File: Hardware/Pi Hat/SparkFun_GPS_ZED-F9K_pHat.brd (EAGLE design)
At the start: 65 x 57.3 mm, 113 parts, among them J1 QWIIC_RIGHT_ANGLE, J2 RASPBERRYPI-40-PIN-GPIO_SMD_S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, J4 U.FL, U1 UBLOX_ZED_F9R, U2 HCPL-270L

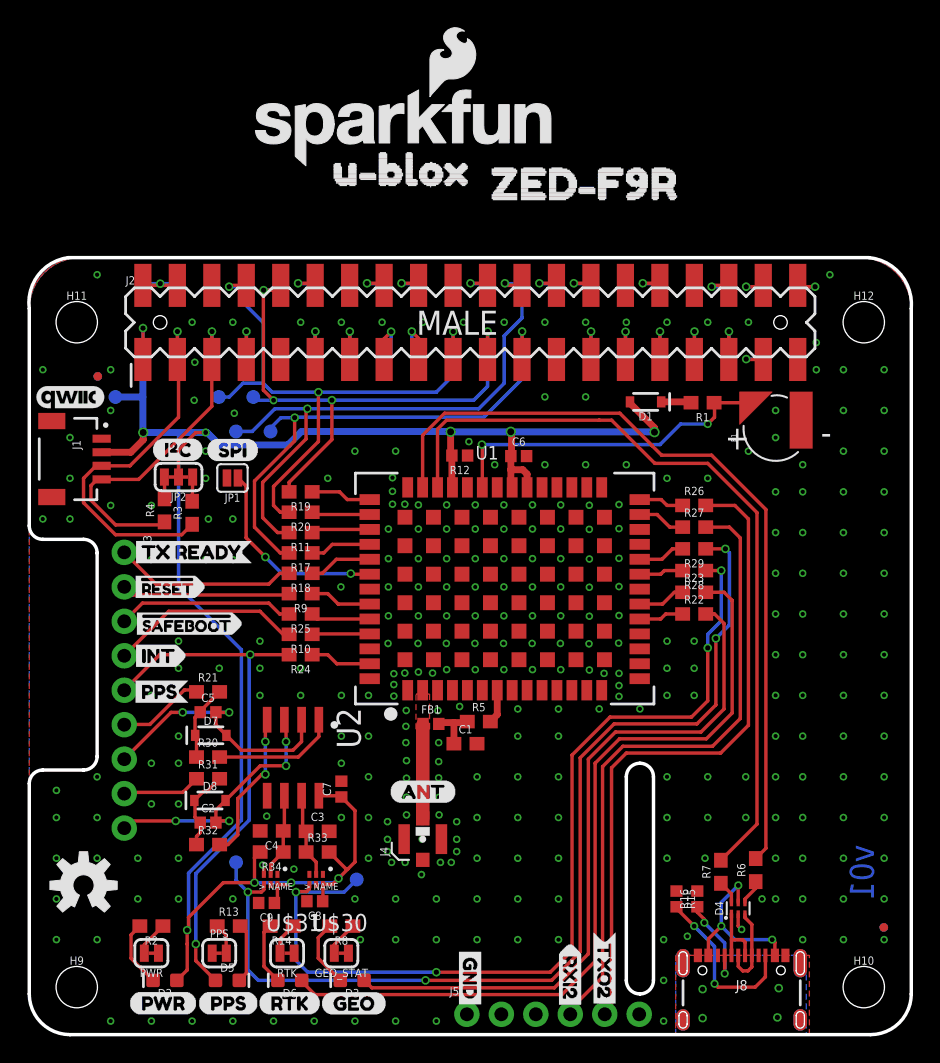
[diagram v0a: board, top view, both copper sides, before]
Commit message: Adds automotive certified diode to wt/dir circuitry
* Adds wt/dir circuitry to both breakout board and pi hat
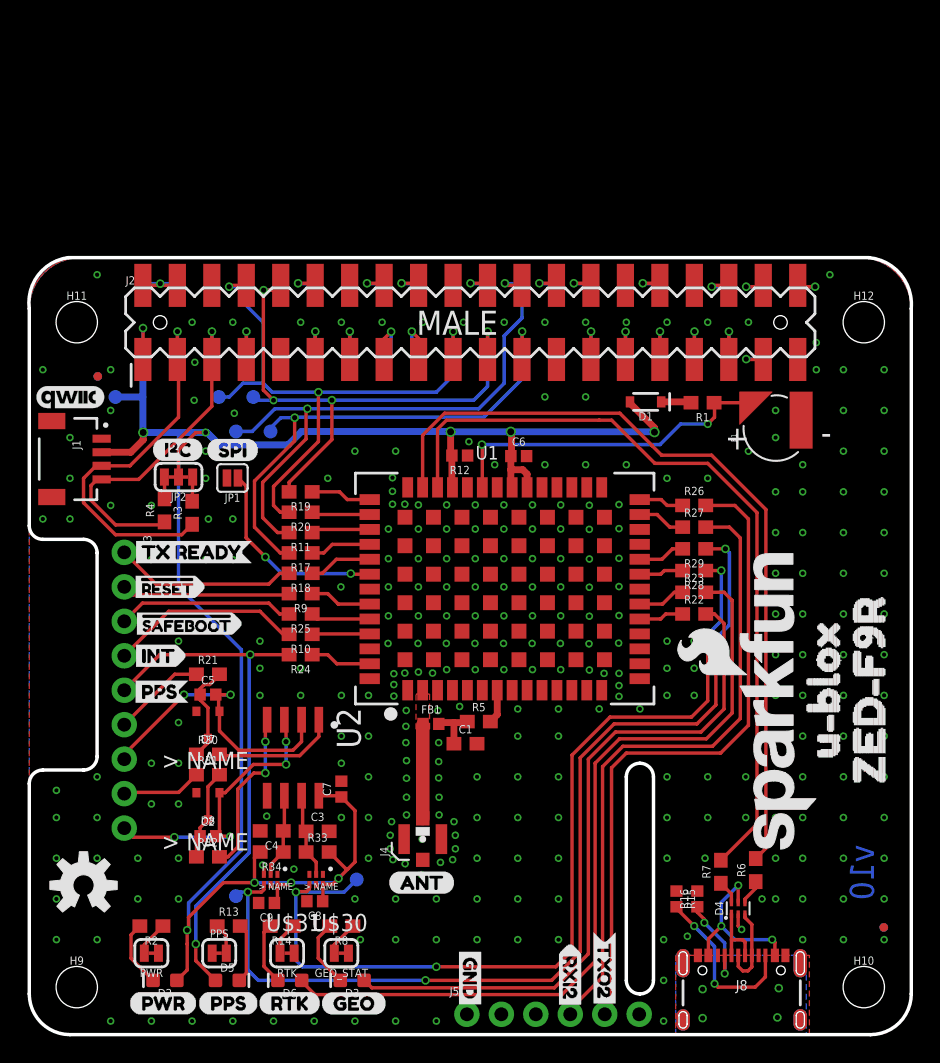
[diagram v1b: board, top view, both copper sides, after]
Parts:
- D7, D8: device SparkFun-DiscreteSemi:SOD-323 -> classified:SOT23_BZX
- moved U$25 59.5 mm to (58.6, 18.3), turned to 90 degrees
- moved U$26 55.0 mm to (61.9, 16.5), turned to 90 degrees
- moved LOGO1 50.4 mm to (55.1, 24.6), turned to 90 degrees
- moved U$21 6.70 mm to (26.4, 11.2)
- moved TP7 2.49 mm to (15.2, 10.2)
- moved R21 1.30 mm to (13.2, 26.6)
- moved C5 1.30 mm to (13.2, 25.1)
- moved C2 1.00 mm to (13.2, 14.6)
- moved R32 0.90 mm to (13.2, 13.1)
- moved D7 0.81 mm to (13.2, 22.8), turned to 180 degrees
- moved D8 0.44 mm to (13.2, 16.8), turned to 180 degrees
- moved R31 0.30 mm to (13.2, 19.2)
- moved R30 0.20 mm to (13.2, 20.7)
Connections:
- net DIR-: now also D8.P1; no longer D8.A
- net N$27: now also D7.P3; no longer D7.C
- net N$36: now also D8.P3; no longer D8.C
- net WT-: now also D7.P1; no longer D7.A
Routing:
- net WT-: track 20.0 -> 22.4 mm
- net DIR-: track 19.9 -> 21.7 mm
- net N$27: track 5.60 -> 7.39 mm
- net DIR_OUT: track 75.0 -> 73.5 mm
- net DIR_IN: track 11.2 -> 12.4 mm
- net N$36: track 6.08 -> 6.91 mm
- net GND: vias 303 -> 299
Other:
- board text added: "v10"
- board text removed: "v01"

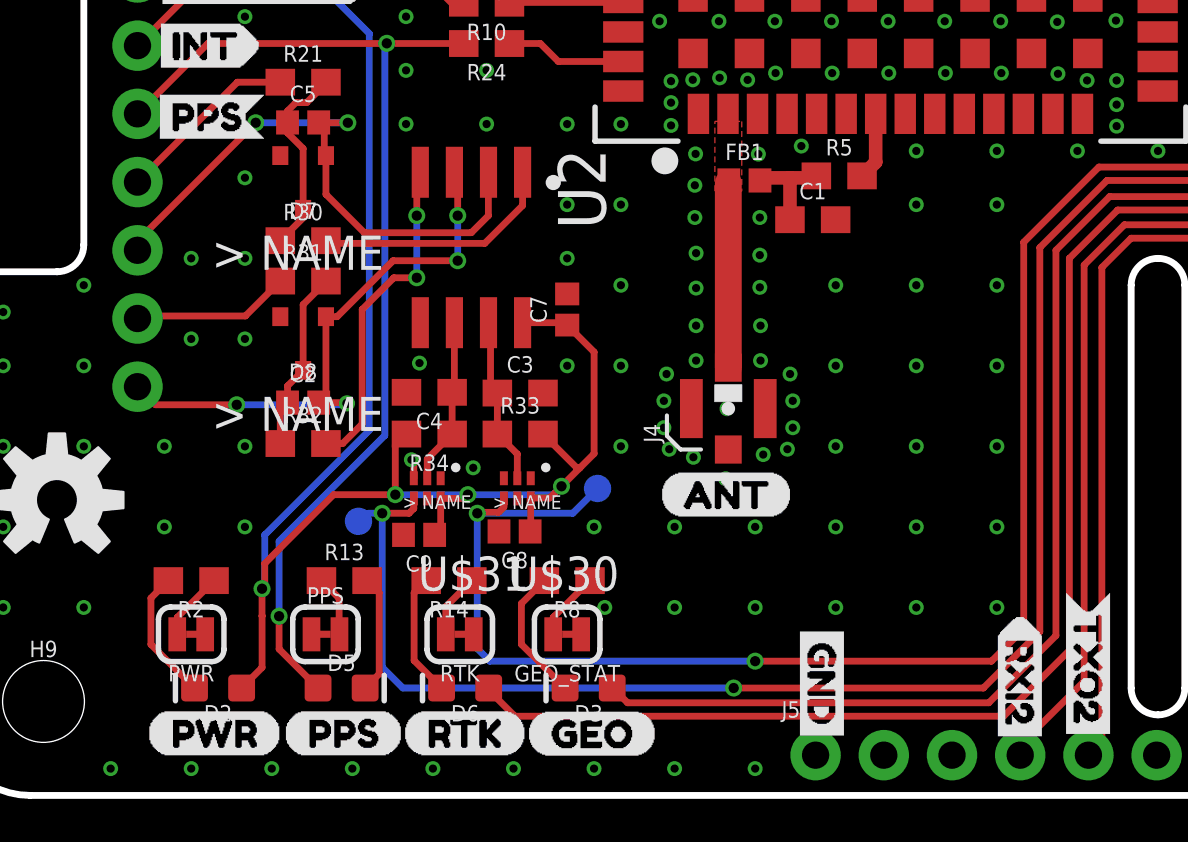
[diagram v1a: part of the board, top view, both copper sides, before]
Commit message: Adds labels for new PTH for wt/dir lines
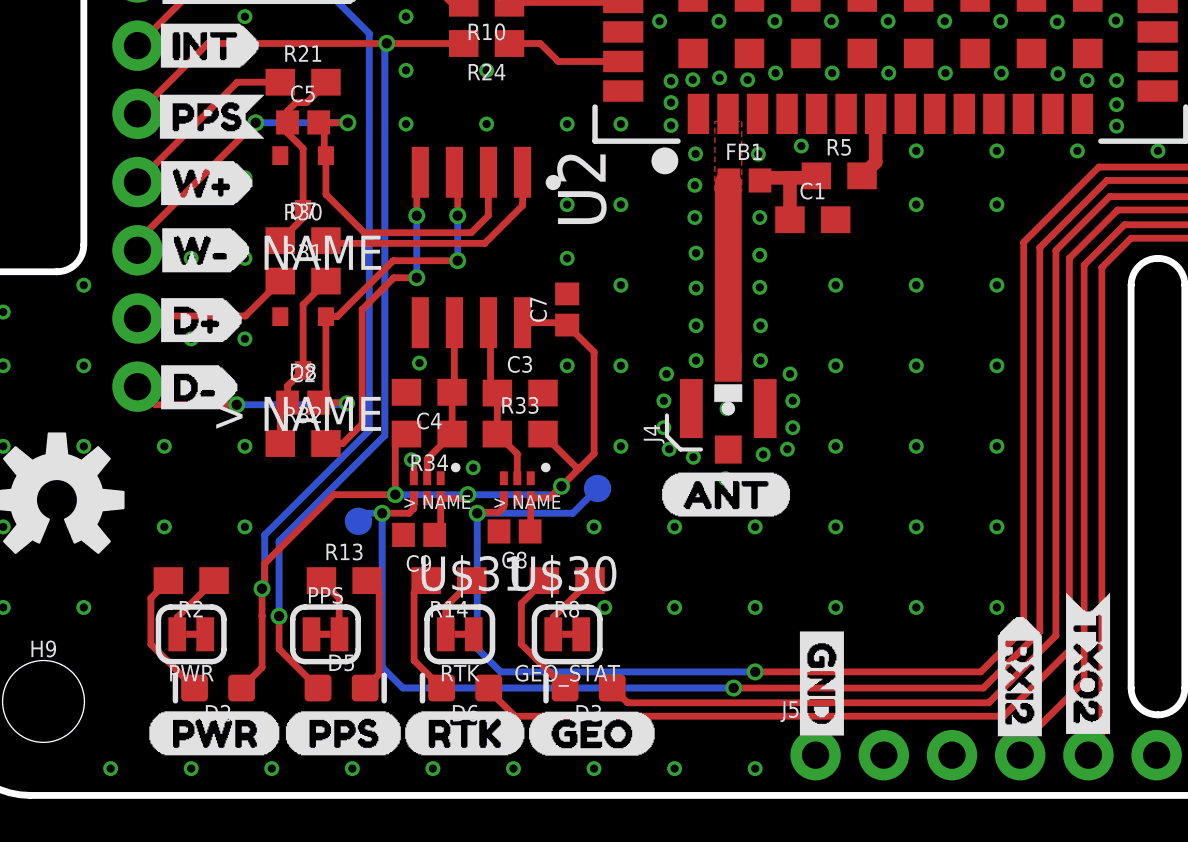
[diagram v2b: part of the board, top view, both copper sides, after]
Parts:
- added U$22: (no value), wt_dir_top:D#0
- added U$23: (no value), wt_dir_top:D#1
- added U$27: (no value), wt_dir_top:W#2
- added U$28: (no value), wt_dir_top:W#3
- added U$32: (no value), wt_dir:D#0
- added U$33: (no value), wt_dir:D#1
- added U$34: (no value), wt_dir:W#2
- added U$35: (no value), wt_dir:W#3
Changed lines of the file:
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@@
 <layer number="19" name="Unrouted" color="6" fill="1" visible="yes" active="yes"/>
 <layer number="20" name="Dimension" color="15" fill="1" visible="yes" active="yes"/>
-<layer number="21" name="tPlace" color="16" fill="1" visible="no" active="yes"/>
-<layer number="22" name="bPlace" color="14" fill="1" visible="no" active="yes"/>
+<layer number="21" name="tPlace" color="16" fill="1" visible="yes" active="yes"/>
+<layer number="22" name="bPlace" color="14" fill="1" visible="yes" active="yes"/>
 <layer number="23" name="tOrigins" color="15" fill="1" visible="yes" active="yes"/>
 <layer number="24" name="bOrigins" color="15" fill="1" visible="yes" active="yes"/>
@@
 <layer number="37" name="tTest" color="7" fill="1" visible="no" active="yes"/>
 <layer number="38" name="bTest" color="7" fill="1" visible="no" active="yes"/>
-<layer number="39" name="tKeepout" color="4" fill="11" visible="yes" active="yes"/>
+<layer number="39" name="tKeepout" color="4" fill="11" visible="no" active="yes"/>
 <layer number="40" name="bKeepout" color="1" fill="11" visible="no" active="yes"/>
 <layer number="41" name="tRestrict" color="4" fill="10" visible="no" active="yes"/>
@@
 <element name="TP6" library="SparkFun-Connectors" package="PAD.03X.04" value="TEST-POINT3X4" x="24.13" y="11.43" smashed="yes" rot="MR270"/>
 <element name="TP7" library="SparkFun-Connectors" package="PAD.03X.04" value="TEST-POINT3X4" x="15.229" y="10.208" smashed="yes" rot="MR270"/>
+<element name="U$22" library="wt_dir_top" package="D#0" value="" x="7.4" y="17.7" smashed="yes"/>
+<element name="U$23" library="wt_dir_top" package="D#1" value="" x="7.4" y="15.2" smashed="yes"/>
+<element name="U$27" library="wt_dir_top" package="W#2" value="" x="7.4" y="22.8" smashed="yes"/>
+<element name="U$28" library="wt_dir_top" package="W#3" value="" x="7.4" y="20.3" smashed="yes"/>
+<element name="U$35" library="wt_dir" package="W#3" value="" x="11.2" y="20.3" smashed="yes" rot="MR0"/>
+<element name="U$32" library="wt_dir" package="D#0" value="" x="10.9" y="15.2" smashed="yes" rot="MR0"/>
+<element name="U$33" library="wt_dir" package="D#1" value="" x="10.8" y="17.7" smashed="yes" rot="MR0"/>
+<element name="U$34" library="wt_dir" package="W#2" value="" x="11.3" y="22.8" smashed="yes" rot="MR0"/>
 </elements>
 <signals>
@@
 <wire x1="48.8" y1="23.4" x2="42.8" y2="23.4" width="0.254" layer="1"/>
 <wire x1="40" y1="20.6" x2="40" y2="6.2" width="0.254" layer="1"/>
-<wire x1="40" y1="6.2" x2="38.8" y2="5" width="0.254" layer="1"/>
+<wire x1="40" y1="6.2" x2="38.4" y2="4.6" width="0.254" layer="1"/>
 <wire x1="42.8" y1="23.4" x2="40" y2="20.6" width="0.254" layer="1"/>
-<via x="30" y="5" extent="1-16" drill="0.381"/>
-<wire x1="20.122" y1="5" x2="30" y2="5" width="0.254" layer="16"/>
+<via x="30" y="4.6" extent="1-16" drill="0.381"/>
+<wire x1="20.522" y1="4.6" x2="30" y2="4.6" width="0.254" layer="16"/>
 <via x="19.652" y="10.508" extent="1-16" drill="0.381"/>
 <contactref element="R28" pad="1"/>
@@
 <wire x1="50" y1="29.5" x2="51" y2="30.5" width="0.254" layer="16"/>
 <wire x1="19.652" y1="10.508" x2="19.652" y2="5.47" width="0.254" layer="16"/>
-<wire x1="19.652" y1="5.47" x2="20.122" y2="5" width="0.254" layer="16"/>
+<wire x1="19.652" y1="5.47" x2="20.522" y2="4.6" width="0.254" layer="16"/>
 <wire x1="19.652" y1="10.508" x2="19.685" y2="10.541" width="0.254" layer="1"/>
 <wire x1="19.685" y1="10.541" x2="20.447" y2="10.541" width="0.254" layer="1"/>
@@
 <wire x1="19.652" y1="10.508" x2="23.208" y2="10.508" width="0.254" layer="16"/>
 <wire x1="23.208" y1="10.508" x2="24.13" y2="11.43" width="0.254" layer="16"/>
-<wire x1="38.8" y1="5" x2="30" y2="5" width="0.254" layer="1"/>
+<wire x1="38.4" y1="4.6" x2="30" y2="4.6" width="0.254" layer="1"/>
 </signal>
 <signal name="DIR_OUT">

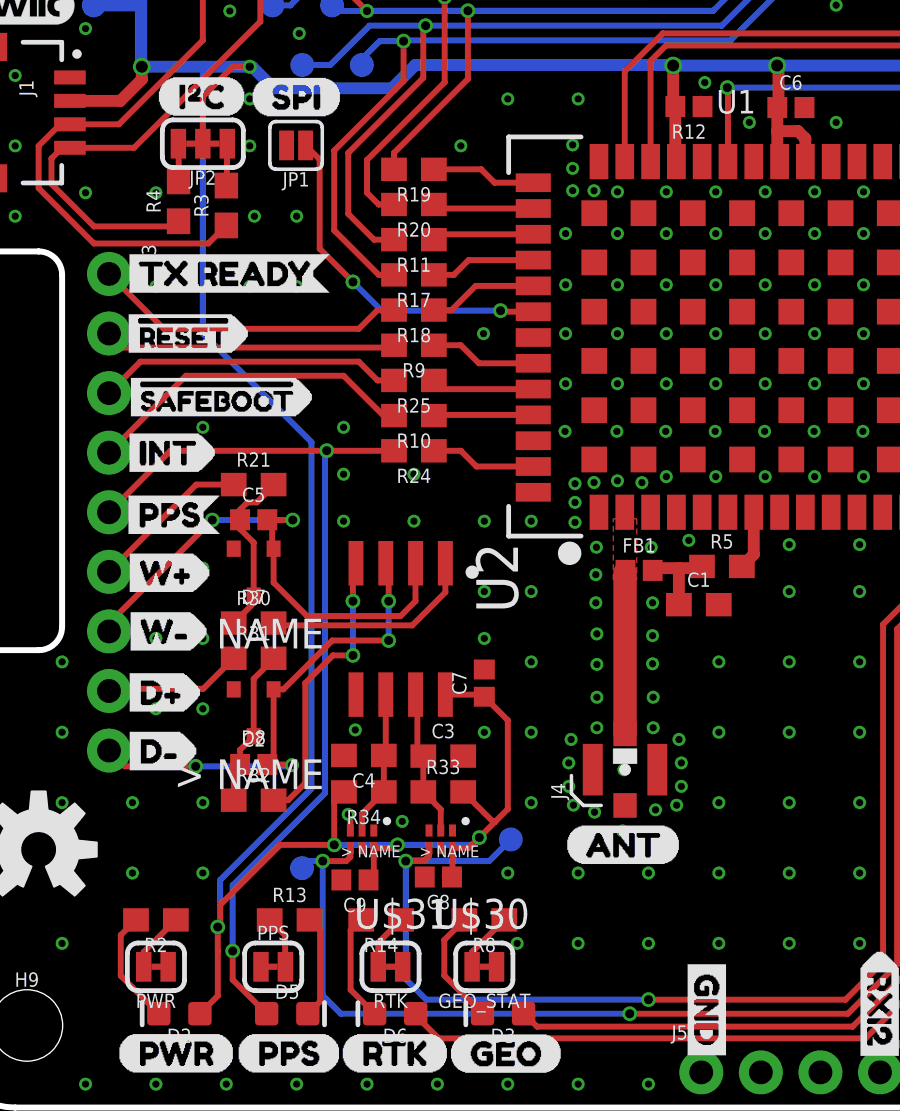
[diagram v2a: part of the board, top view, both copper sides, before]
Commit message: Updates designs with new X7R capacitors
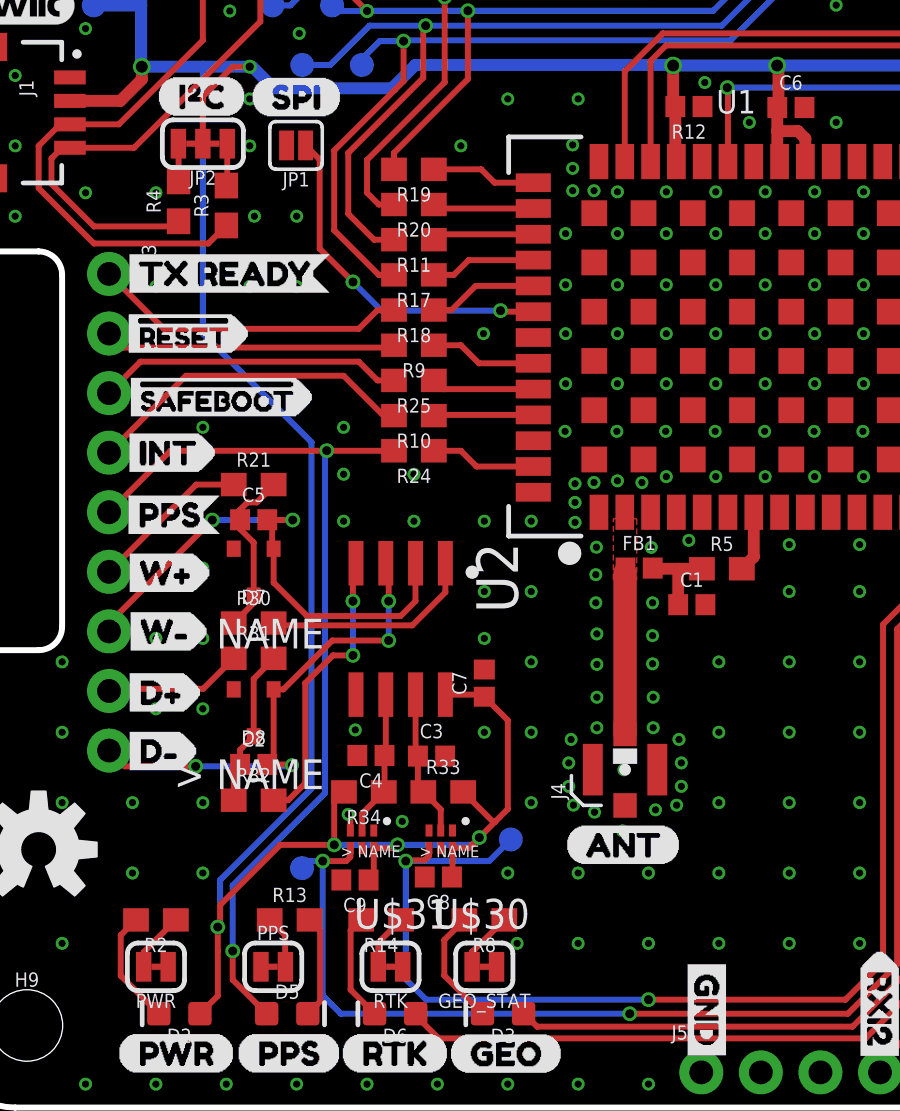
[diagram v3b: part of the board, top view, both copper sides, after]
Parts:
- C1, C3, C4: device SparkFun-Capacitors:0603 -> SparkFun-Capacitors:0402
- C2, C5: value 1.0nF -> 1nF
- moved C3 0.50 mm to (20.8, 15.0)
- moved C1 0.30 mm to (31.8, 21.4)
- moved C4 0.30 mm to (18.2, 15.0)
- moved FB1 0.10 mm to (29.6, 23.0)
- moved R5 0.10 mm to (33.1, 23.0)
